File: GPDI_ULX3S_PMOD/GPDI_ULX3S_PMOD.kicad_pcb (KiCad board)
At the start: 4 copper layers, 40 x 23.8 mm, 51 parts, among them J2 PMOD, P1 HDMI-D, U1 RN5RK501A, U2 PCA9306

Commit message: New panel
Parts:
- added G***: LOGO, parts2:OSH_7x7, F.Cu at (139.3, 76.2)
- added G***: LOGO, parts2:radiona-12mm, F.Cu at (117.9, 86.8)
- moved L1 0.25 mm to (139.5, 87.0)
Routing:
- net GND: track 162.5 -> 174.7 mm, vias 36 -> 39
- net Net-(D1-Pad2): track 12.4 -> 13.3 mm
- added copper zone on F.Cu, net GND
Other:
- board outline removed

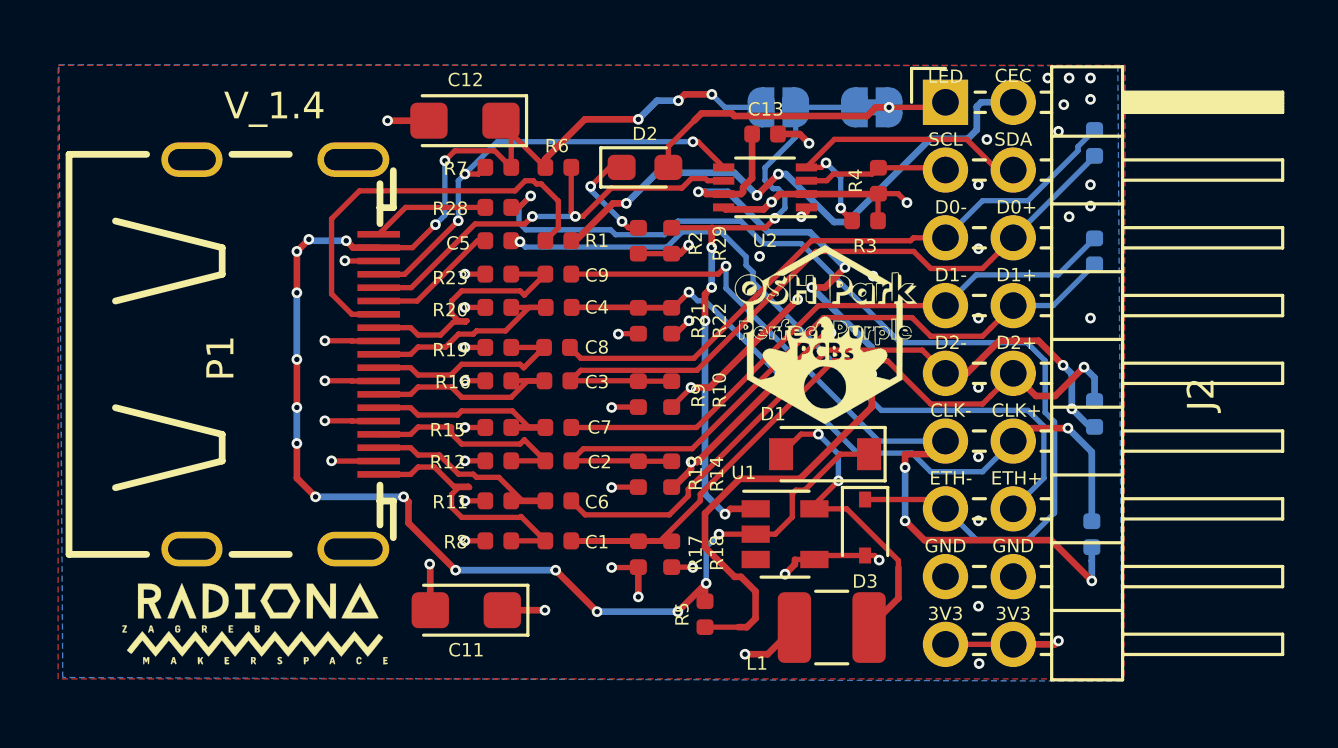
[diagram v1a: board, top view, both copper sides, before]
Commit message: Changing GPDI connector as used on ULX3S
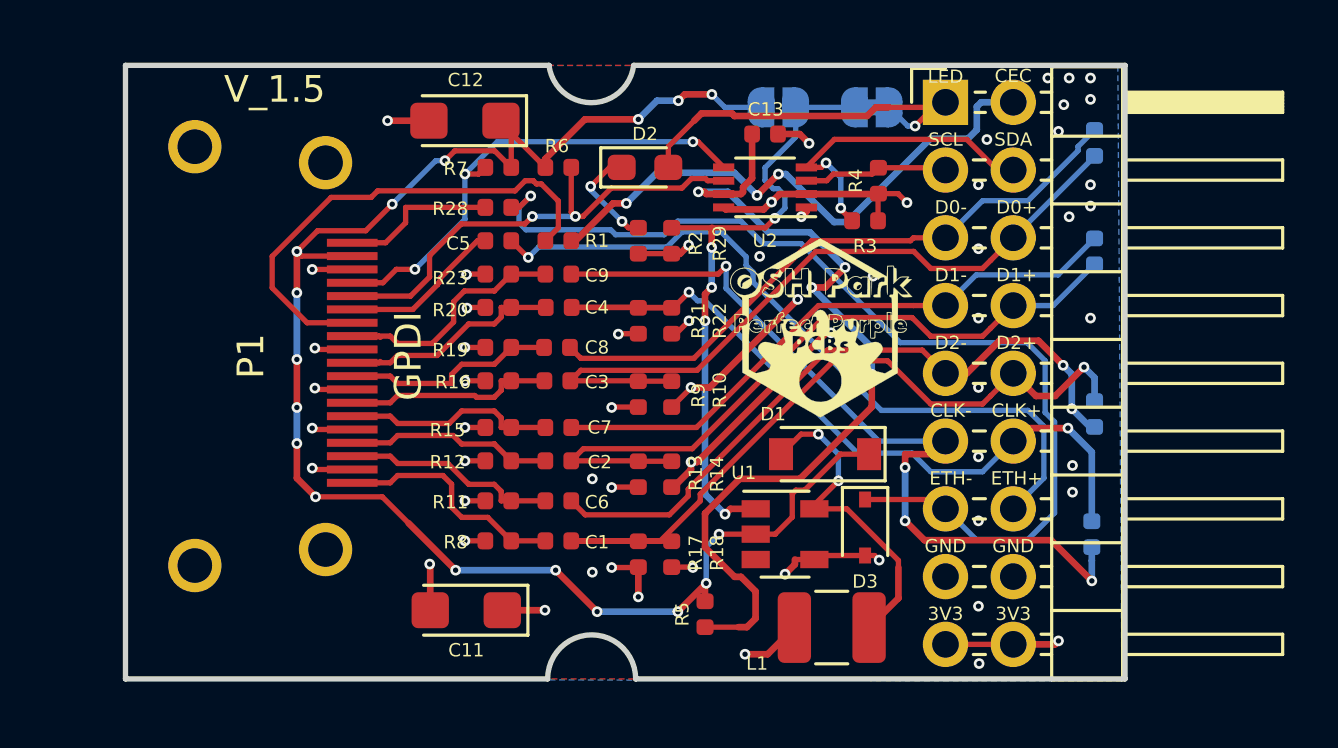
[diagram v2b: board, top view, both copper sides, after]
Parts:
- removed the G*** at (117.9, 86.8)
- added G***: LOGO, parts2:radiona-16mm, B.Cu at (131.8, 77.4)
- P1: value HDMI-D -> GPDI; footprint HDMI:HDMI-D -> GPDI:CONN-10029449-111RLF
- moved P1 3.56 mm to (120.5, 76.8), turned to 270 degrees
- moved G*** 0.31 mm to (139.1, 75.9)
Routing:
- net LED_HDMI: track 11.9 -> 14.7 mm
- net /CEC: track 16.0 -> 18.6 mm
- net GND: track 174.7 -> 177.1 mm, vias 39 -> 43
- net GPDI_SCL: track 16.6 -> 18.2 mm
- net /D2+: track 10.4 -> 8.87 mm
- net /ETH-: track 4.42 -> 5.88 mm
- net GPDI_SDA: track 17.1 -> 18.4 mm
- net /ETH+: track 4.93 -> 6.15 mm
- net /CLK-: track 10.2 -> 8.95 mm
- net /D1+: track 8.45 -> 7.75 mm
- net +5V: track 62.2 -> 62.4 mm, vias 20 -> 17
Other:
- board outline added: 37.5 x 23 mm
- board text added: "V_1.5"
- board text removed: "V_1.4"

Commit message: Adding GPDI version 1.5
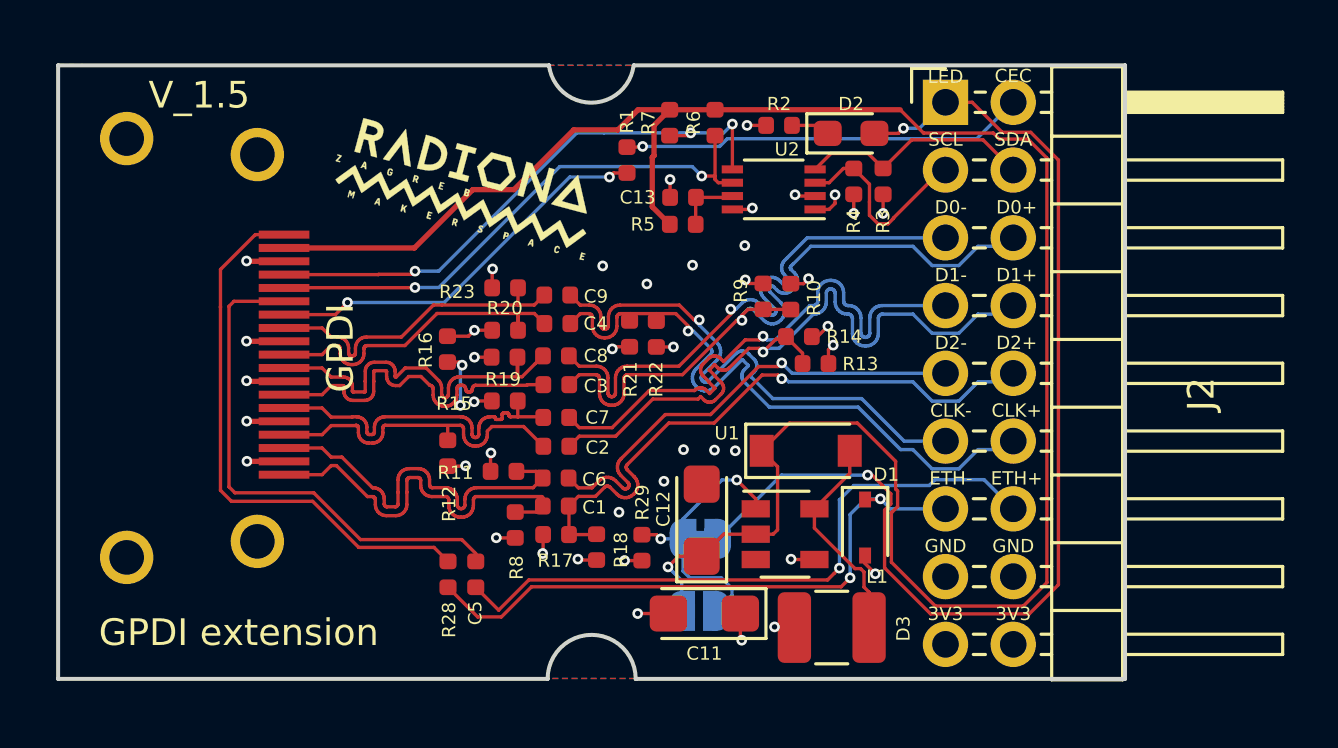
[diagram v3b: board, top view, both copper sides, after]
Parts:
- removed the G*** at (131.8, 77.4)
- removed the G*** at (139.1, 75.9)
- removed P1: GPDI, GPDI:CONN-10029449-111RLF
- removed R24, R25, R26, R27: 200R, Resistor_SMD:R_0402_1005Metric
- added G***: LOGO, parts2:shutleworth-12mm, B.Cu at (126.9, 80.6)
- added G***: LOGO, parts2:radiona-10mm, B.Cu at (115.8, 76.8)
- added G***: LOGO, parts2:OSH_10x10, B.Cu at (137.0, 73.6)
- added G***: LOGO, parts2:radiona-10mm, F.Cu at (125.8, 70.5)
- added GPDI: GPDI, GPDI:CONN-10029449-111RLF, F.Cu at (118.0, 76.5)
- J2: value PMOD -> CONN
- moved JP2 19.1 mm to (134.5, 86.4)
- moved C12 17.4 mm to (134.6, 83.0), turned to 90 degrees
- moved JP1 17.4 mm to (134.6, 83.7)
- moved R5 14.6 mm to (133.9, 71.9), turned to 0 degrees
- moved R28 13.9 mm to (125.1, 85.0), turned to 270 degrees
- moved C5 12.5 mm to (126.2, 85.0), turned to 90 degrees
- moved R29 11.6 mm to (132.4, 84.0)
- moved C11 8.93 mm to (134.7, 86.5)
- moved D2 7.83 mm to (140.2, 68.5)
- moved R13 7.83 mm to (138.9, 77.1), turned to 180 degrees
- moved R14 7.02 mm to (138.3, 76.1), turned to 0 degrees
- moved R2 6.82 mm to (137.5, 68.2), turned to 180 degrees
- moved R7 6.64 mm to (133.4, 68.1), turned to 270 degrees
- moved R6 6.11 mm to (135.1, 68.1), turned to 270 degrees
- moved R9 5.94 mm to (136.9, 74.6), turned to 270 degrees
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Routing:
- net GND: track 177.1 -> 19.9 mm, vias 43 -> 25
- net +3V3: track 51.0 -> 13.5 mm, vias 18 -> 17
- net Net-(C13-Pad1): track 33.0 -> 2.40 mm, vias 4 -> 0
- net LED_HDMI: track 14.7 -> 43.2 mm, vias 1 -> 2
- net +5V: track 62.4 -> 87.5 mm, vias 17 -> 1
- net GPDI_ETH-: track 38.4 -> 23.1 mm, vias 1 -> 2
- net /ETH-: track 5.88 -> 20.9 mm
- net /ETH+: track 6.15 -> 19.5 mm
- net Net-(JP1-Pad2): track 23.8 -> 10.7 mm, vias 5 -> 2
- net GPDI_CLK-: track 30.8 -> 21.0 mm, vias 4 -> 1
- net /D0+: track 7.81 -> 15.7 mm, vias 0 -> 2
- net GPDI_D2-: track 25.5 -> 17.8 mm, vias 2 -> 1
- net /D2-: track 8.14 -> 14.8 mm
- net GPDI_CEC: track 21.4 -> 15.2 mm, vias 3 -> 1
- net GPDI_D2+: track 29.3 -> 23.1 mm
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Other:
- board size 37.5 x 23 mm -> 40 x 23 mm
- net class Default: clearance 0.2 -> 0.127; trace_width 0.25 -> 0.127; via_dia 0.8 -> 0.4; via_drill 0.4 -> 0.2
- rule pad_to_mask_clearance: 0.051 -> 0
- rule trace_clearance: 0.2 -> 0.127
- rule trace_min: 0.2 -> 0.127
- board text added: "GPDI extension"

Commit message: Adding changes
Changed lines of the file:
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@@
       (drillshape 0)
       (scaleselection 1)
-      (outputdirectory "Gerber/new"))
+      (outputdirectory "Gerber/"))
   )
   (net 0 "")
@@
       (effects (font (size 0.8 0.8) (thickness 0.12)))
     )
-    (pad 1 smd roundrect (at -1.35 0 180) (size 1.4 1.35) (layers F.Cu F.Paste F.Mask) (roundrect_rratio 0.185185)
+    (pad 1 smd roundrect (at -1.35 0 180) (size 1.4 1.35) (layers F.Cu F.Paste F.Mask) (roundrect_rratio 0.1851844444444445)
       (net 2 +3V3))
-    (pad 2 smd roundrect (at 1.35 0 180) (size 1.4 1.35) (layers F.Cu F.Paste F.Mask) (roundrect_rratio 0.185185)
+    (pad 2 smd roundrect (at 1.35 0 180) (size 1.4 1.35) (layers F.Cu F.Paste F.Mask) (roundrect_rratio 0.1851844444444445)
       (net 1 GND))
     (model ${KISYS3DMOD}/Capacitor_Tantalum_SMD.3dshapes/CP_EIA-3216-12_Kemet-S.step
@@
       (effects (font (size 0.5 0.5) (thickness 0.12)))
     )
-    (pad 1 smd roundrect (at -1.35 0 90) (size 1.4 1.35) (layers F.Cu F.Paste F.Mask) (roundrect_rratio 0.185185)
+    (pad 1 smd roundrect (at -1.35 0 90) (size 1.4 1.35) (layers F.Cu F.Paste F.Mask) (roundrect_rratio 0.1851844444444445)
       (net 3 +5V))
-    (pad 2 smd roundrect (at 1.35 0 90) (size 1.4 1.35) (layers F.Cu F.Paste F.Mask) (roundrect_rratio 0.185185)
+    (pad 2 smd roundrect (at 1.35 0 90) (size 1.4 1.35) (layers F.Cu F.Paste F.Mask) (roundrect_rratio 0.1851844444444445)
       (net 1 GND))
     (model ${KISYS3DMOD}/Capacitor_Tantalum_SMD.3dshapes/CP_EIA-3216-12_Kemet-S.step
